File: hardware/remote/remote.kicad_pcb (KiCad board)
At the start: 2 copper layers, 45.7 x 25.4 mm, 16 parts, among them J1 5V, J2 Conn_01x02, SW1 SW_Push, U1 ATtiny85-20PU, U2 LM7805_TO220

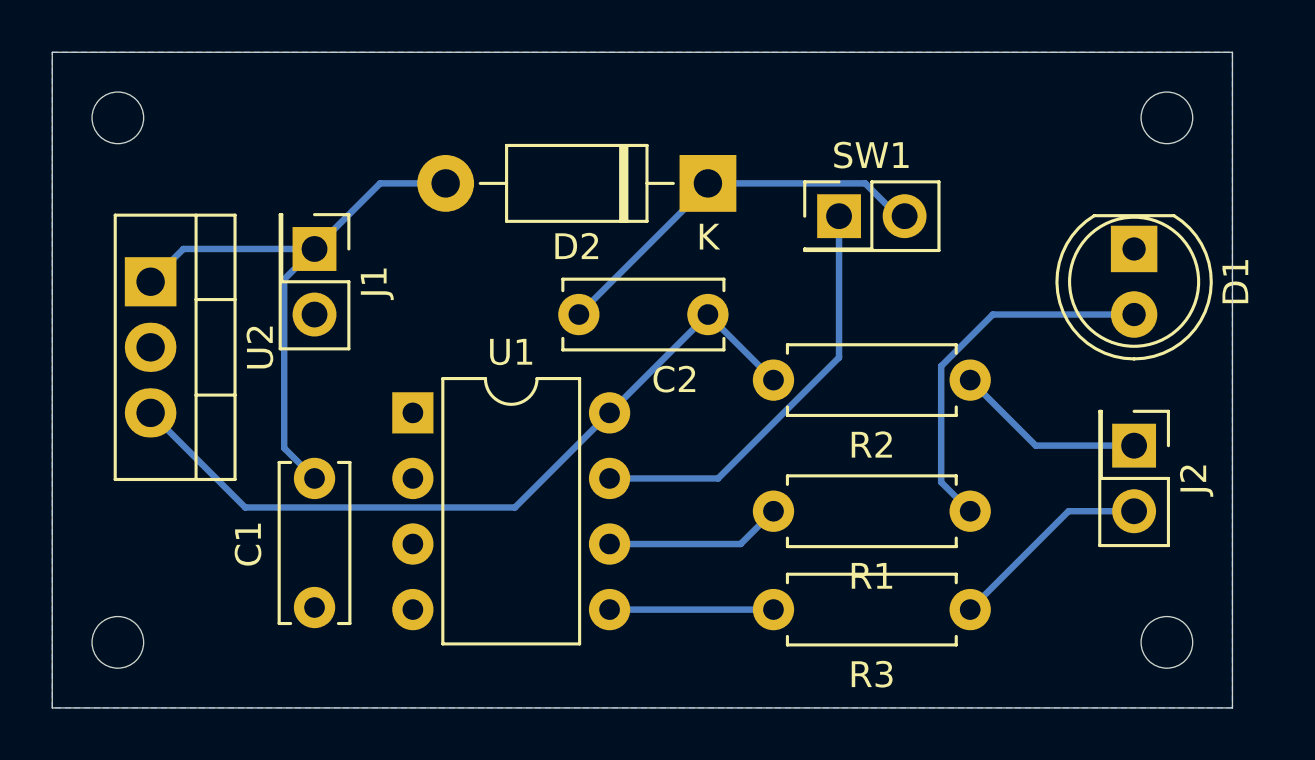
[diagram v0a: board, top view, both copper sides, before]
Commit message: [hardware] Improved PCB layout
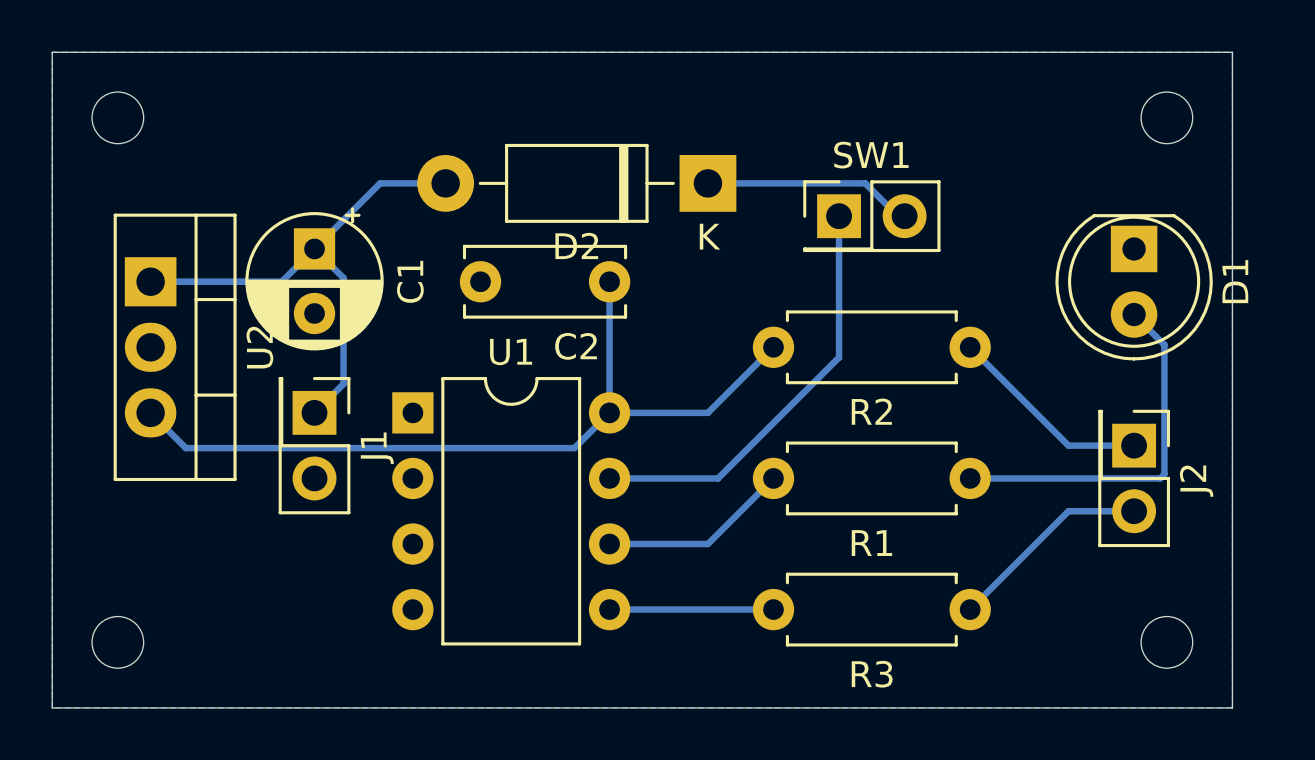
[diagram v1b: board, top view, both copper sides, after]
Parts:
- C1: footprint Capacitor_THT:C_Disc_D6.0mm_W2.5mm_P5.00mm -> Capacitor_THT:CP_Radial_D5.0mm_P2.50mm
- moved C1 8.89 mm to (30.5, 27.9)
- moved J1 6.35 mm to (30.5, 34.3)
- moved C2 4.02 mm to (41.9, 29.2)
- moved R1 1.27 mm to (55.9, 36.8)
- moved R2 1.27 mm to (55.9, 31.8)
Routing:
- net GNDREF: track 15.4 -> 8.34 mm
- net Net-(C1-Pad1): track 22.9 -> 20.3 mm
- net Net-(C2-Pad1): track 29.8 -> 31.4 mm
- net Net-(J2-Pad1): track 7.40 -> 7.93 mm
- net Net-(R1-Pad2): track 6.88 -> 7.40 mm
